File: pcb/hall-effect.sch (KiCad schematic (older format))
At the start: 6 parts

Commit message: moved motor driver away from i2c bus
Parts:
- 5V?: symbol generic:5V -> pcb-rescue:5V-generic
- CN?: symbol pin_headers:1x3 -> pcb-rescue:1x3-pin_headers
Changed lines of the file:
@@
 $EndComp
 $Comp
-L generic:5V 5V?
+L pcb-rescue:5V-generic 5V?
 U 1 1 5E98F7C0
 P 5600 3700
@@
 	5700 4000 5400 4000
 $Comp
-L pin_headers:1x3 CN?
+L pcb-rescue:1x3-pin_headers CN?
 U 1 1 5E98F7CB
 P 5400 3900

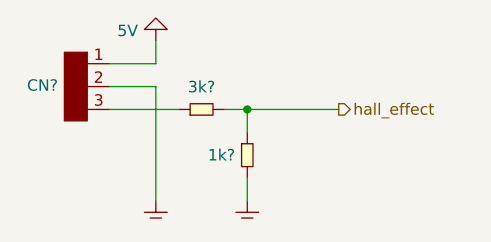
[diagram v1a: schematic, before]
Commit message: added resistor & capacitor values
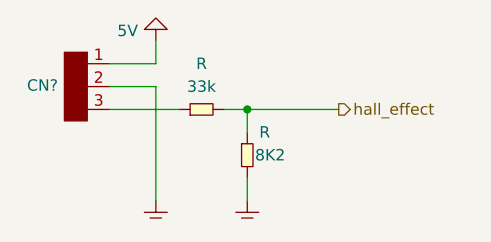
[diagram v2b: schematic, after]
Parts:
- R: renamed from 1k?; value R -> 8K2
- R: renamed from 3k?; value R -> 33k
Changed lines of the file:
@@
 $EndDescr
 $Comp
-L generic:R 1k?
+L generic:R R
 U 1 1 5E98F7A1
 P 6000 4200
-F 0 "1k?" V 6000 4253 50  0000 L CNN
-F 1 "R" H 6000 4100 50  0001 C CNN
+F 0 "R" V 5900 4100 50  0000 L CNN
+F 1 "8K2" V 6000 4100 50  0000 C CNN
 F 2 "SMT:0603" H 5900 4175 50  0001 C CNN
 F 3 "" H 6000 4200 50  0001 C CNN
@@
 $EndComp
 $Comp
-L generic:R 3k?
+L generic:R R
 U 1 1 5E98F7A8
 P 5800 4000
-F 0 "3k?" H 5800 3902 50  0000 C CNN
-F 1 "R" H 5800 3900 50  0001 C CNN
+F 0 "R" H 5800 3800 50  0000 C CNN
+F 1 "33k" H 5800 3900 50  0000 C CNN
 F 2 "SMT:0603" H 5700 3975 50  0001 C CNN
 F 3 "" H 5800 4000 50  0001 C CNN

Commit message: fixed schematic symbols being rescued from cache
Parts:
- 5V?: symbol pcb-rescue:5V-generic -> generic:5V
- CN?: symbol pcb-rescue:1x3-pin_headers -> pin_headers:1x3
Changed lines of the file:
@@
 $EndComp
 $Comp
-L pcb-rescue:5V-generic 5V?
+L generic:5V 5V?
 U 1 1 5E98F7C0
 P 5600 3700
@@
 	5700 4000 5400 4000
 $Comp
-L pcb-rescue:1x3-pin_headers CN?
+L pin_headers:1x3 CN?
 U 1 1 5E98F7CB
 P 5400 3900

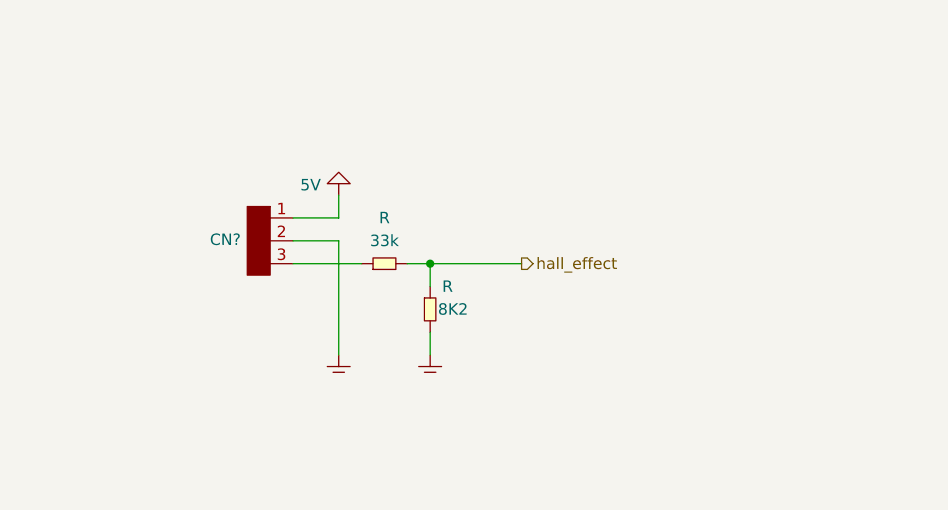
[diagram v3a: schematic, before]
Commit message: changed hall-effect circuit to use two comparators with analog inputs as triggering levels
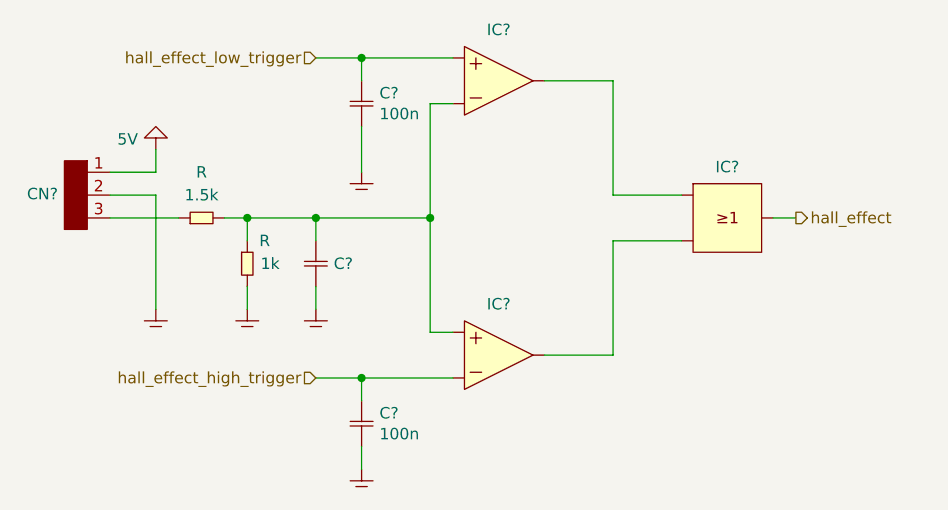
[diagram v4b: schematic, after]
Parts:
- added C? (x2): 100n, SMT:0603, symbol generic:C
- added C?: C, SMT:0603, symbol generic:C
- added GND? (x3): GND, symbol generic:GND
- added IC? (x2): OpAmp, symbol generic:OpAmp
- added IC?: OR, symbol generic:OR
- R: value 8K2 -> 1k
- R: value 33k -> 1.5k
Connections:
- net GND: now also C?.2, C?.2, C?.2, GND?.~ (GND), GND?.~ (GND), GND?.~ (GND)
- net hall_effect: now also IC?.~; no longer R.1, R.2
- new net: C?.1, IC?.~, IC?.~, R.1, R.2
- new net: IC?.~, IC?.~ (x2)
- new net hall_effect_high_trigger: C?.1, IC?.~
- new net hall_effect_low_trigger: C?.1, IC?.~
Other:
- moved on the sheet: CN?, R

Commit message: added DAC to schematic
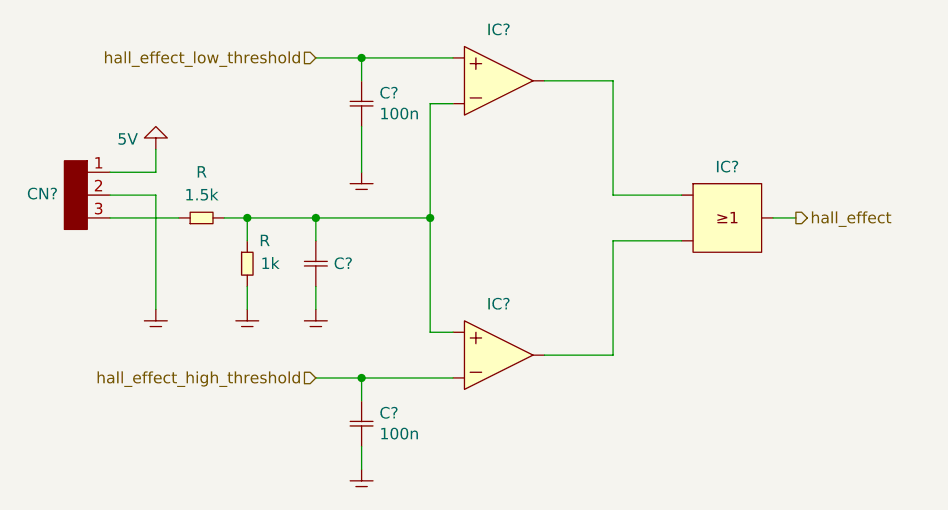
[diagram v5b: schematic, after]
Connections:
- net hall_effect_high_trigger is gone; now on net hall_effect_high_threshold: C?.1, IC?.~
- net hall_effect_low_trigger is gone; now on net hall_effect_low_threshold: C?.1, IC?.~
- net hall_effect_low_threshold: now reaches IC?.~
- net hall_effect_low_threshold: no longer IC?.~
- net hall_effect_high_threshold: now reaches IC?.~
- net hall_effect_high_threshold: no longer IC?.~
- new net: IC?.~, IC?.~ (x2)
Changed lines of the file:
@@
 	5700 3100 5700 3200
 Text HLabel 5500 3100 0    50   Input ~ 0
-hall_effect_low_trigger
+hall_effect_low_threshold
 Wire Wire Line
 	5500 3100 5700 3100
 Connection ~ 5700 3100
 Text HLabel 5500 4500 0    50   Input ~ 0
-hall_effect_high_trigger
+hall_effect_high_threshold
 Wire Wire Line
 	5500 4500 5700 4500
